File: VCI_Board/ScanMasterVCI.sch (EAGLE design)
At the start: 74 parts, among them IC1 XMEGA16A4A, Q1 MMBT3904, Q13 MMBT3904, Q14 MMBT3904, Q15 MMBT3904, Q16 MMBT3904, Q17 MMBT3904, Q3 MMBT3904, Q4 MMBT4403, Q6 MMBT3904, Q7 ZXMP6A17G, Q8 MMBT4403, U1 MAX17502FATB+, U2 SN65HVDA195-Q1, U3 MAX17502EATB+, U4 L78L08ABUTR

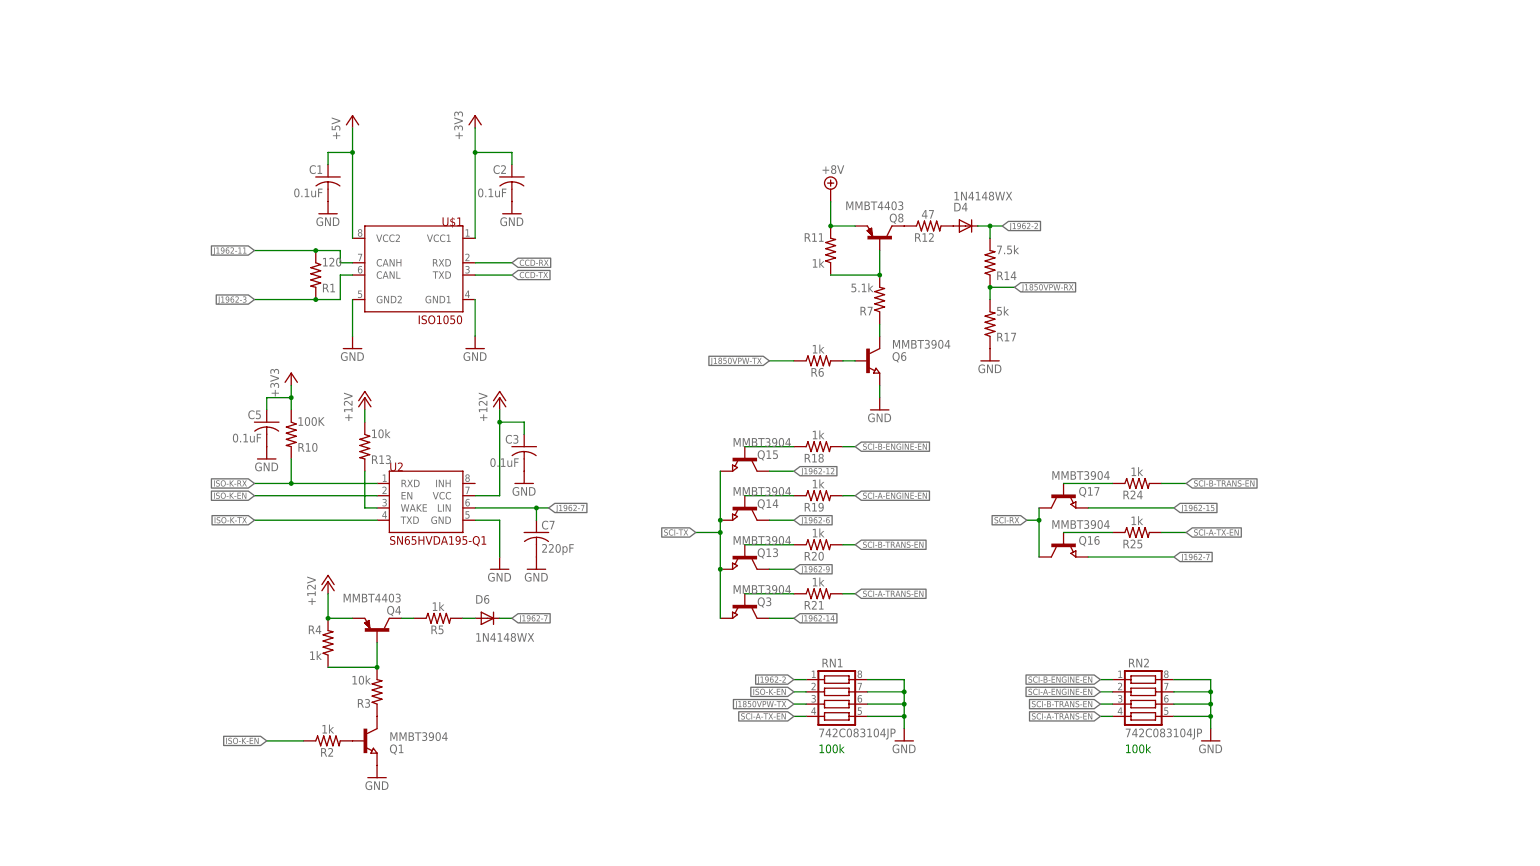
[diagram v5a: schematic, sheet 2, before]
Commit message: Added MOSFETs for muxing. Adding transistors and diodes to protect SCI from the ISO9141 voltage was getting tedious, so I've implemented proper multiplexing using 2 MOSFET IC's I've seen used before. They're both N-channel. Also noticed that the datasheet for the SN65HVDA195-Q1 specifies a series resistor and capacitor to ground for ISO-K-TX for noise filtering and overcurrent protection.
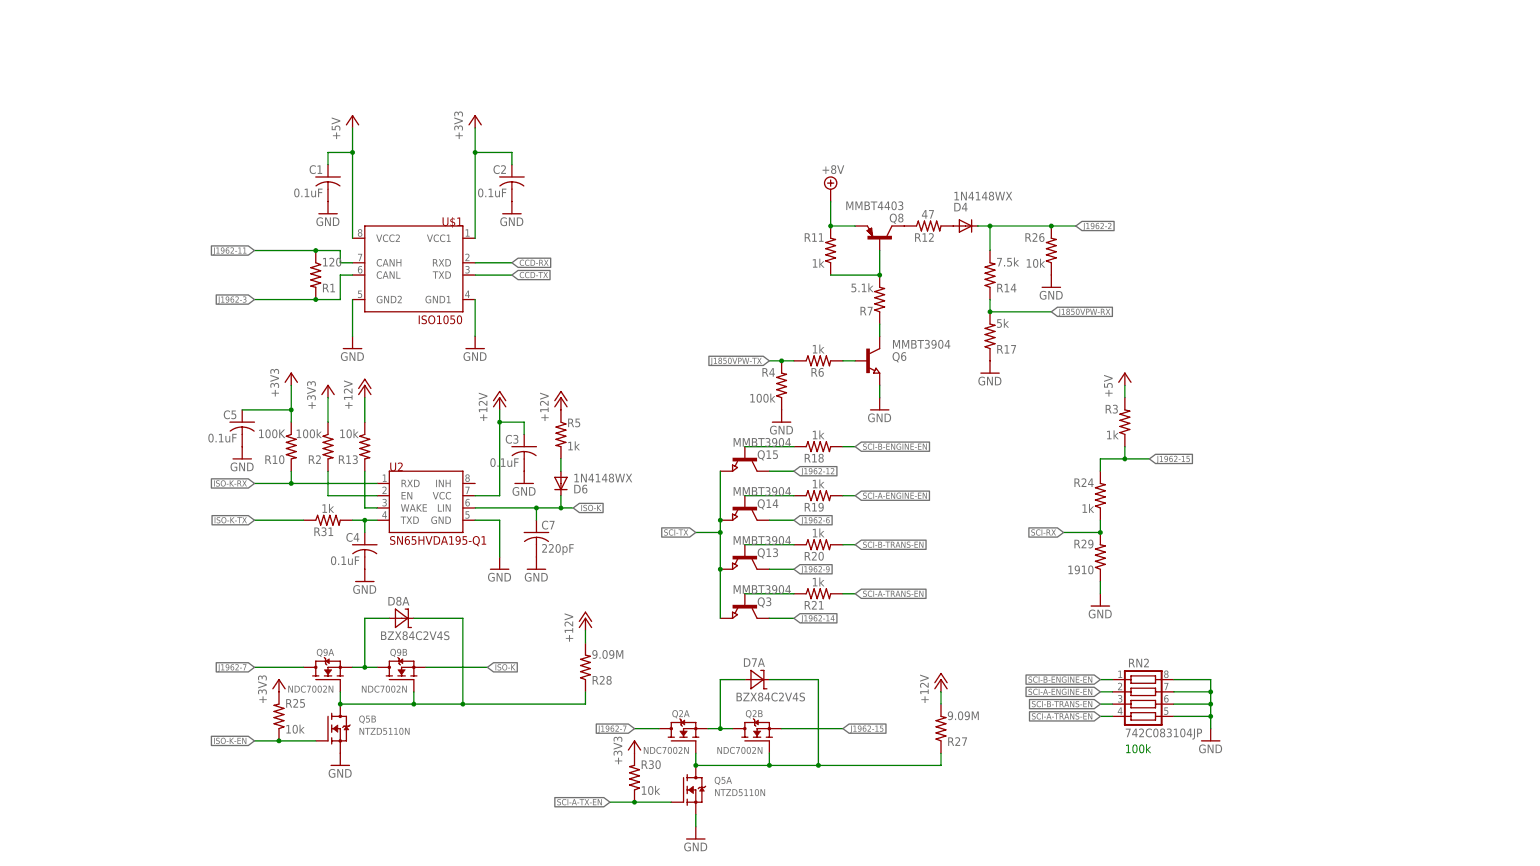
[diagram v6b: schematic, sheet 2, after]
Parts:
- removed Q1, Q16, Q17: MMBT3904, semicon-smd-ipc:NPN-TRANSISTOR_SOT23
- removed Q4: MMBT4403, transistor-pnp:MMBT4403LT1SMD
- removed RN1: 742C083104JP, resistor-net:CTS742C083
- added C4: 0.1uF, adafruit:C-USC0805
- added D7, D8: BZX84C2V4S, customics:BZX84C2V4S
- added Q2, Q9: NDC7002N, customics:NDC7002N
- added Q5: NTZD5110N, customics:NTZD5110N
- added R26, R30: 10k, adafruit:R-US_R0805
- added R27, R28: 9.09M, adafruit:R-US_R0805
- added R29: 1910, adafruit:R-US_R0805
- added R31: 1k, adafruit:R-US_R0805
- R2, R4: value 1k -> 100k
- R25: value 1k -> 10k
- R3: value 10k -> 1k
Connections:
- removed net N$11: Q4.B, R3.2, R4.1
- removed net N$24: Q17.B, R24.1
- removed net N$25: Q16.B, R25.1
- removed net N$27: Q4.C, R5.1
- new net ISO-K: C7.1, D6.C, Q9B.S, U2.LIN
- new net N$1: D7A.A, Q2A.S, Q2B.D
- new net N$2: D7A.C, Q2A.G, Q2B.G, Q5A.D, R27.1
- new net N$4: D8A.A, Q9A.S, Q9B.D
- new net N$5: D8A.C, Q5B.D, Q9A.G, Q9B.G, R28.1
- net +12V: now also R27.2, R28.2, R5.1; no longer Q4.E, R4.2
- net +3V3: now also R2.1, R25.2, R30.2
- net +5V: now also R3.2
- net GND: now also C4.2, Q5A.S, Q5B.S, R26.1, R29.1, R4.1; no longer Q1.E, RN1.5, RN1.6, RN1.7, RN1.8
- net ISO-K-EN: now also Q5B.G, R25.1; no longer R2.1, RN1.2, U2.EN
- net ISO-K-TX: now also R31.1; no longer U2.TXD
- net J1850VPW-TX: now also R4.2; no longer RN1.3
- net J1962-15: now also Q2B.S, R24.2, R3.1; no longer Q17.E
- net J1962-2: now also R26.2; no longer RN1.1
- net J1962-7: now also Q2A.D, Q9A.D; no longer C7.1, D6.C, Q16.E, U2.LIN
- net N$10: now also C4.1, R31.2, U2.TXD; no longer Q1.C, R3.1
- net N$8: now also U2.EN; no longer Q1.B
- net SCI-A-TX-EN: now also Q5A.G, R30.1; no longer R25.2, RN1.4
- net SCI-B-TRANS-EN: no longer R24.2
- net SCI-RX: now also R24.1, R29.2; no longer Q16.C, Q17.C
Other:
- moved on the sheet: C5, D6, R10, R14, R17, R2, R24, R25, R3, R4, R5

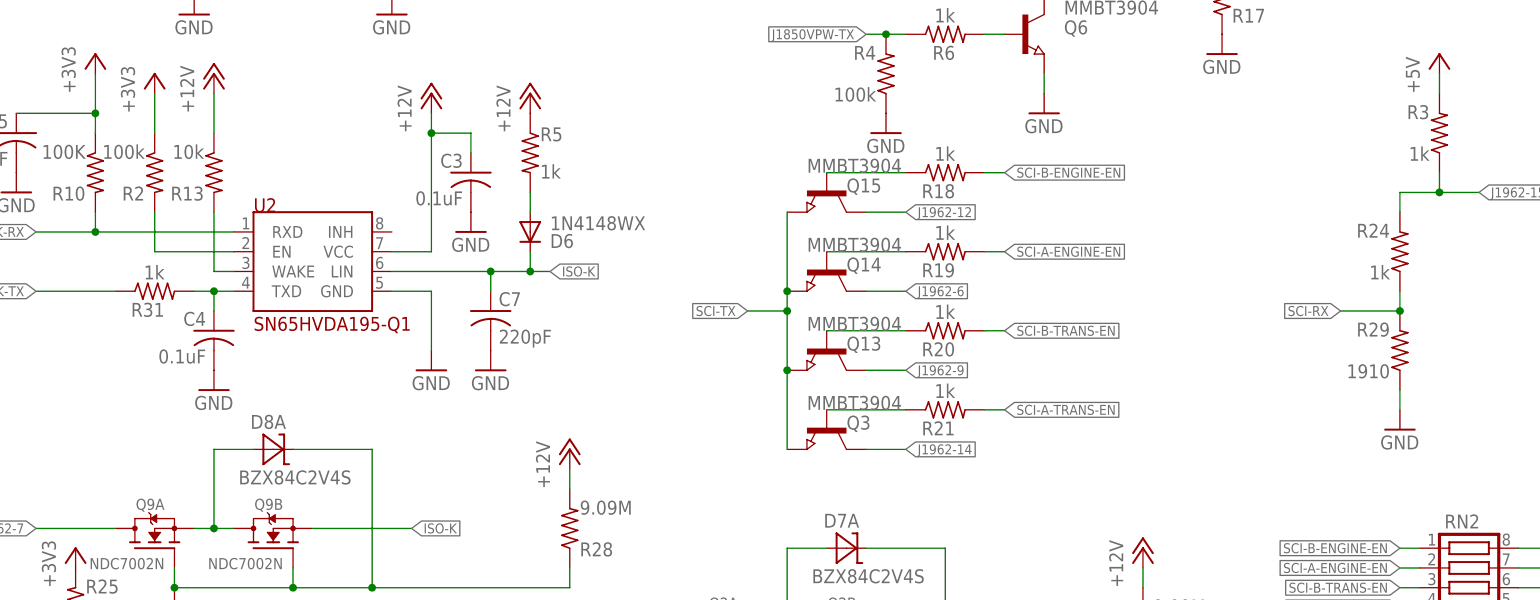
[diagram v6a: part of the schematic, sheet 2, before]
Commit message: Made a quick pass at a board layout. Added .brd file with only the components placed on the board. Layout isn't completely final. Changed the resistor package size to 0603...I'll just plan on using a reflow oven.
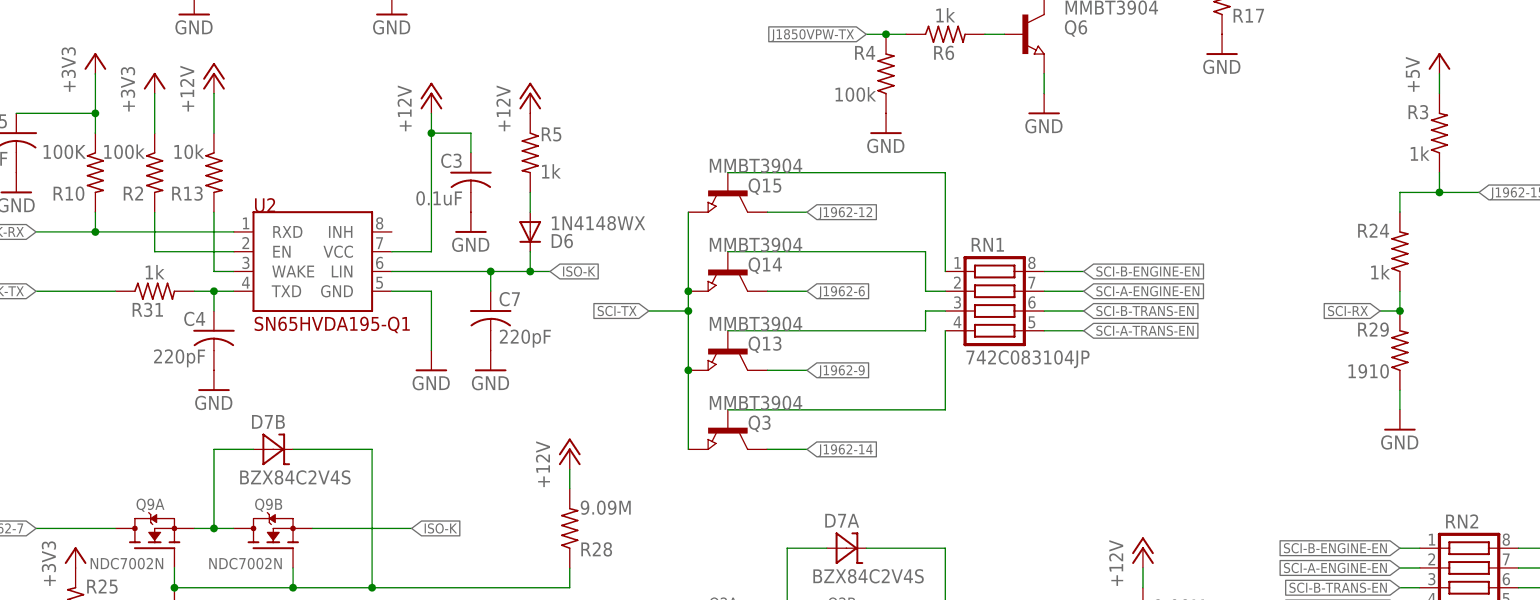
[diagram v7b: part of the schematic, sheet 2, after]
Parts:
- removed D8: BZX84C2V4S, customics:BZX84C2V4S
- removed R18, R19, R20, R21: 1k, adafruit:R-US_R0805
- added RN1: 742C083104JP, resistor-net:CTS742C083
- C10, C11, C12, C13, C14, C15, C17, C18, C19, C2, C3, C5, C7, C8, C9: device adafruit:C-USC0805 -> adafruit:C-USC0603
- C4: value 0.1uF -> 220pF; device adafruit:C-USC0805 -> adafruit:C-USC0603
- R1, R10: device adafruit:R-US_R0805W -> adafruit:R-US_R0603
- R11, R12, R13, R14, R15, R16, R17, R2, R22, R23, R24, R25, R26, R27, R28, R29, R3, R30, R31, R4, R5, R6, R7, R8, R9: device adafruit:R-US_R0805 -> adafruit:R-US_R0603
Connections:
- net J1962-2: now also J1962_1.2
- net N$13: now also RN1.1; no longer R18.1
- net N$21: now also RN1.2; no longer R19.1
- net N$22: now also RN1.3; no longer R20.1
- net N$23: now also RN1.4; no longer R21.1
- net N$4: now also D7B.A; no longer D8A.A
- net N$5: now also D7B.C; no longer D8A.C
- net SCI-A-ENGINE-EN: now also RN1.7; no longer R19.2
- net SCI-A-TRANS-EN: now also RN1.5; no longer R21.2
- net SCI-B-ENGINE-EN: now also RN1.8; no longer R18.2
- net SCI-B-TRANS-EN: now also RN1.6; no longer R20.2
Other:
- moved on the sheet: Q13, Q14, Q15, Q3
